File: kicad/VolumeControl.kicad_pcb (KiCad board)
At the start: 2 copper layers, 160 x 59.1 mm, 67 parts, among them IC1 ATMEGA328P-P, P1 PWR_IN, P10 ICSP, P2 SOURCE_1, P3 SOURCE_2, P4 RS232, P5 VOL_KNOB, P6 PI_PWR, P7 PA_EN, P8 FRONT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

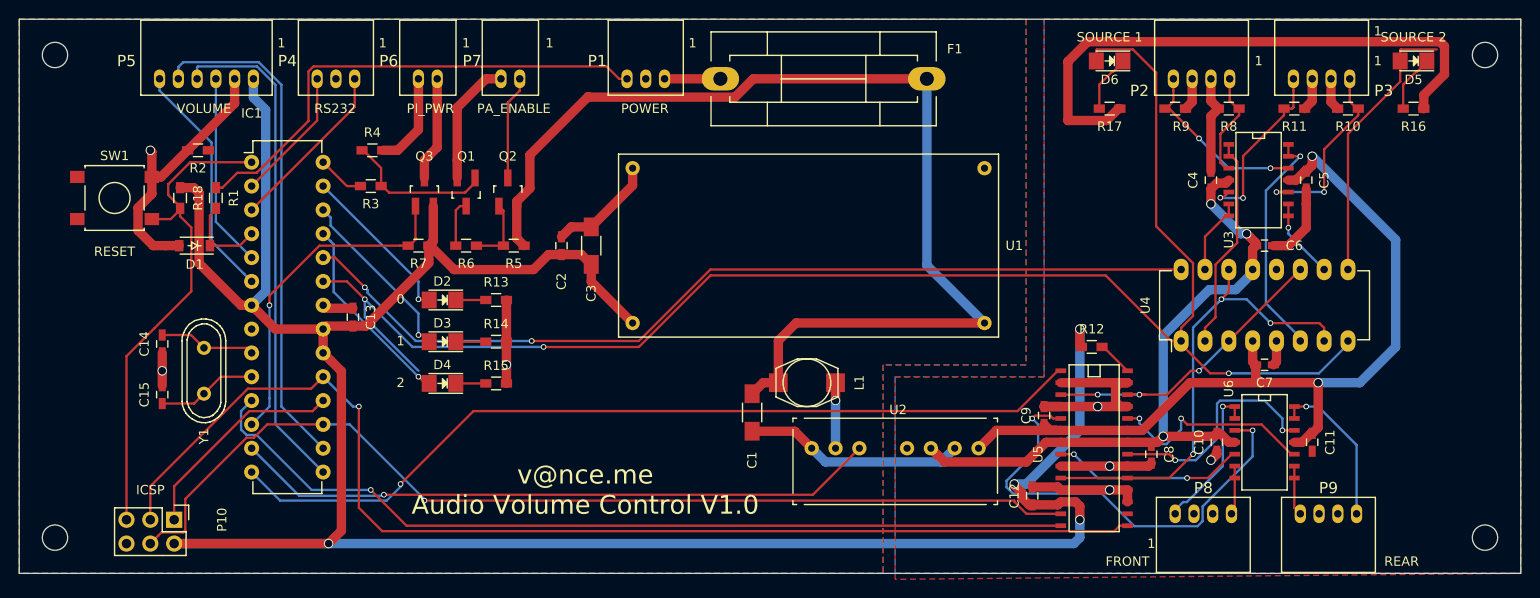
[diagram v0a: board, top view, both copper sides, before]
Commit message: Updated to include extra indicator LEDs controlled by the ATMega.  PCB reworked
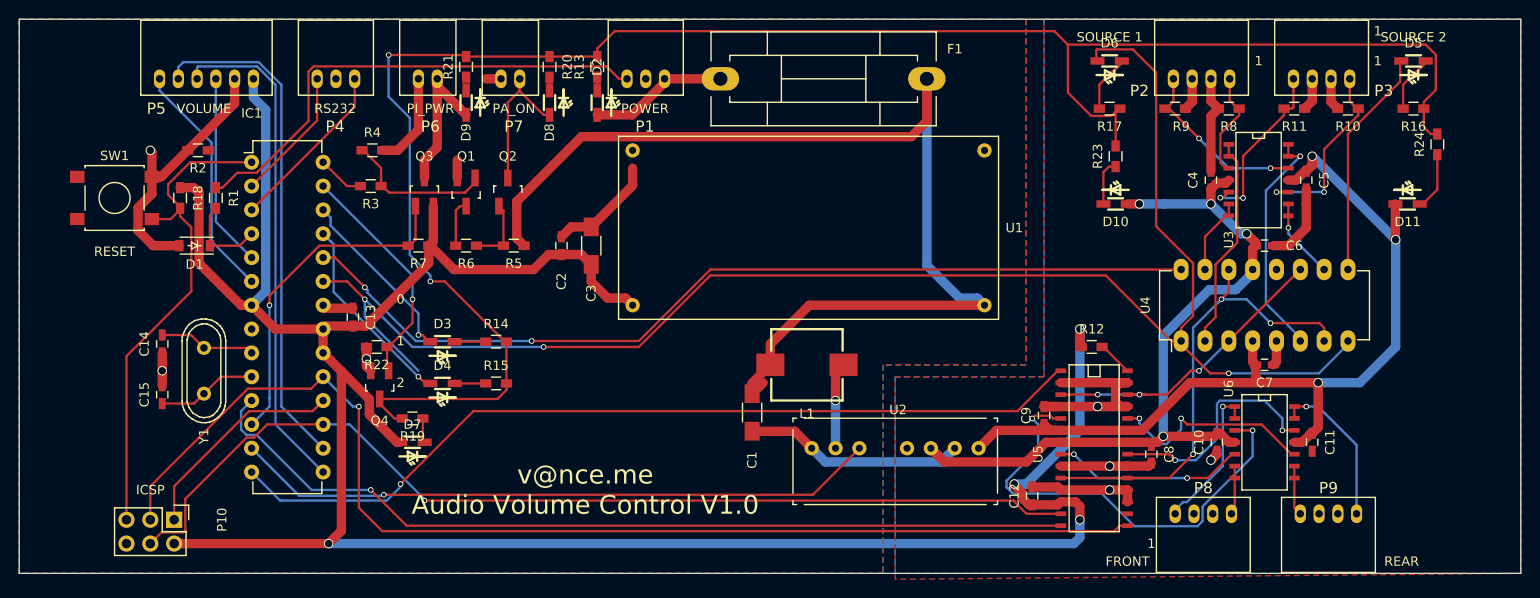
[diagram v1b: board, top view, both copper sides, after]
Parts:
- removed REF** (x4): MountingHole_2.7mm_M2.5_ISO7380, Mounting_Holes:MountingHole_2.7mm_M2.5_ISO7380
- added D10: +5VA, SMD_LED:LED_SMD_1.6x0.8mm, F.Cu at (173.4, 70.5)
- added D11: -5VA, SMD_LED:LED_SMD_1.6x0.8mm, F.Cu at (204.5, 70.5)
- added D7: +5VD, SMD_LED:LED_SMD_1.6x0.8mm, F.Cu at (98.4, 95.9)
- added D8: PA, SMD_LED:LED_SMD_1.6x0.8mm, F.Cu at (113.0, 59.7)
- added D9: PI, SMD_LED:LED_SMD_1.6x0.8mm, F.Cu at (104.1, 59.7)
- added Q4: NXP2301P, TO_SOT_Packages_SMD:SOT-23_Handsoldering, F.Cu at (94.9, 89.8)
- added R19: 220, Resistors_SMD:R_0603_HandSoldering, F.Cu at (98.4, 93.3)
- added R20: 1k, Resistors_SMD:R_0603_HandSoldering, F.Cu at (113.0, 55.9)
- added R21: 220, Resistors_SMD:R_0603_HandSoldering, F.Cu at (104.1, 55.9)
- added R22: 10k, Resistors_SMD:R_0603_HandSoldering, F.Cu at (94.6, 85.7)
- added R23: 220, Resistors_SMD:R_0603_HandSoldering, F.Cu at (173.4, 65.4)
- added R24: 220, Resistors_SMD:R_0603_HandSoldering, F.Cu at (207.6, 64.1)
- D2: value 0 -> +12V; footprint LEDs:LED_1206 -> SMD_LED:LED_SMD_1.6x0.8mm
- D3, D4, D5, D6: footprint LEDs:LED_1206 -> SMD_LED:LED_SMD_1.6x0.8mm
- L1: footprint Inductors:SELF-WE-PD3S -> Inductor_SRR0735A:Inductor_SRR0735A
- Q2, Q3: value Si2301BDS -> NX2301P
- R13: value 220 -> 1k
- moved R13 27.1 mm to (118.1, 55.9), turned to 90 degrees
- moved D2 26.7 mm to (118.1, 59.7), turned to 270 degrees
- moved L1 1.91 mm to (140.5, 87.6)
- moved U1 1.89 mm to (141.4, 81.3)
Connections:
- D2 pad 2: Net-(D2-Pad2) -> /Power/+12V_SUPPLY
- IC1 pad 27: Net-(D2-Pad2) -> Net-(IC1-Pad27)
- R13 pad 2: GND -> LED_GND
- R14 pad 2: GND -> LED_GND
- R15 pad 2: GND -> LED_GND
- R16 pad 2: GND -> LED_GND
- R17 pad 2: GND -> LED_GND
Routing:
- net LED_GND: track 0.00 -> 199.8 mm, vias 0 -> 2
- net GND: track 241.6 -> 164.3 mm
- net Net-(IC1-Pad27): track 0.00 -> 24.9 mm, vias 0 -> 1
- net Net-(D2-Pad2): track 17.4 -> 0.00 mm, vias 1 -> 0
- net /Power/+12V_SUPPLY: track 5.95 -> 15.4 mm
- net +5VA: track 71.4 -> 80.2 mm, vias 3 -> 4
- net Net-(D11-Pad2): track 0.00 -> 6.23 mm
- net +5VD: track 270.7 -> 265.1 mm
- net /Power/+12V_PA_ENABLE: track 11.1 -> 16.6 mm
- net /Power/+5V_PI: track 11.1 -> 16.2 mm
- net /Audio Processing/SOURCE_2_ENABLE: track 128.1 -> 123.0 mm
- net Net-(D10-Pad1): track 0.00 -> 4.93 mm
- net -5VA: track 91.4 -> 95.2 mm, vias 2 -> 3
- net Net-(D7-Pad1): track 0.00 -> 2.62 mm
- net Net-(L1-Pad2): track 6.98 -> 9.24 mm
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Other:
- board text added: "PA_ON"
- board text removed: "PA_ENABLE"

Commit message: Minor updates and board submitted for fabrication
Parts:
- added D12: RX, SMD_LED:LED_SMD_1.6x0.8mm, F.Cu at (67.9, 66.0)
- added D13: TX, SMD_LED:LED_SMD_1.6x0.8mm, F.Cu at (67.9, 69.2)
- added D14: MISO, SMD_LED:LED_SMD_1.6x0.8mm, F.Cu at (67.9, 98.4)
- added D15: MOSI, SMD_LED:LED_SMD_1.6x0.8mm, F.Cu at (67.9, 94.6)
- added R25: 220, Resistors_SMD:R_0603_HandSoldering, F.Cu at (63.5, 66.0)
- added R26: 220, Resistors_SMD:R_0603_HandSoldering, F.Cu at (63.5, 69.2)
- added R27: 220, Resistors_SMD:R_0603_HandSoldering, F.Cu at (63.5, 98.4)
- added R28: 220, Resistors_SMD:R_0603_HandSoldering, F.Cu at (63.5, 94.6)
- added REF**: MountingHole_2.7mm_M2.5_ISO7380_Pad, Mounting_Holes:MountingHole_2.7mm_M2.5_ISO7380_Pad, F.Cu at (60.3, 54.6)
- added REF**: MountingHole_2.7mm_M2.5_ISO7380_Pad, Mounting_Holes:MountingHole_2.7mm_M2.5_ISO7380_Pad, F.Cu at (60.3, 106.0)
- added REF**: MountingHole_2.7mm_M2.5_ISO7380_Pad, Mounting_Holes:MountingHole_2.7mm_M2.5_ISO7380_Pad, F.Cu at (212.7, 106.0)
- added REF**: MountingHole_2.7mm_M2.5_ISO7380_Pad, Mounting_Holes:MountingHole_2.7mm_M2.5_ISO7380_Pad, F.Cu at (212.7, 54.6)
- Q4: value NXP2301P -> TSM2302CX
- moved SW1 5.72 mm to (66.7, 75.6)
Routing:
- net LED_GND: track 199.8 -> 286.0 mm, vias 2 -> 5
- net /DIgital_Control/TX_OUT: track 18.5 -> 57.4 mm, vias 0 -> 1
- net /DIgital_Control/RX_IN: track 14.3 -> 45.5 mm, vias 0 -> 1
- net GND: track 164.3 -> 186.9 mm, vias 7 -> 10
- net /Audio Processing/SOURCE_2_ENABLE: track 123.0 -> 145.5 mm, vias 2 -> 3
- net /DIgital_Control/IGNITION: track 9.21 -> 20.9 mm, vias 0 -> 1
- net /Audio Processing/SOURCE_1_ENABLE: track 170.7 -> 160.8 mm
- net /Audio Processing/SDI: track 108.7 -> 118.3 mm, vias 1 -> 3
- net /DIgital_Control/RESET: track 53.1 -> 62.2 mm
- net /DIgital_Control/MISO: track 23.2 -> 28.4 mm, vias 0 -> 2
- net Net-(D15-Pad1): track 0.00 -> 2.05 mm
- net Net-(D14-Pad1): track 0.00 -> 2.05 mm
- net Net-(D13-Pad1): track 0.00 -> 2.05 mm
- net Net-(D12-Pad1): track 0.00 -> 2.05 mm
- net +5VA: track 80.2 -> 81.9 mm
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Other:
- board text added: "+5VA"
- board text added: "+5VD"
- board text added: "-5VA"
- board text added: "MISO"
- board text added: "MOSI"
- board text added: "RX"
- board text added: "TX"
- board text removed: "0"

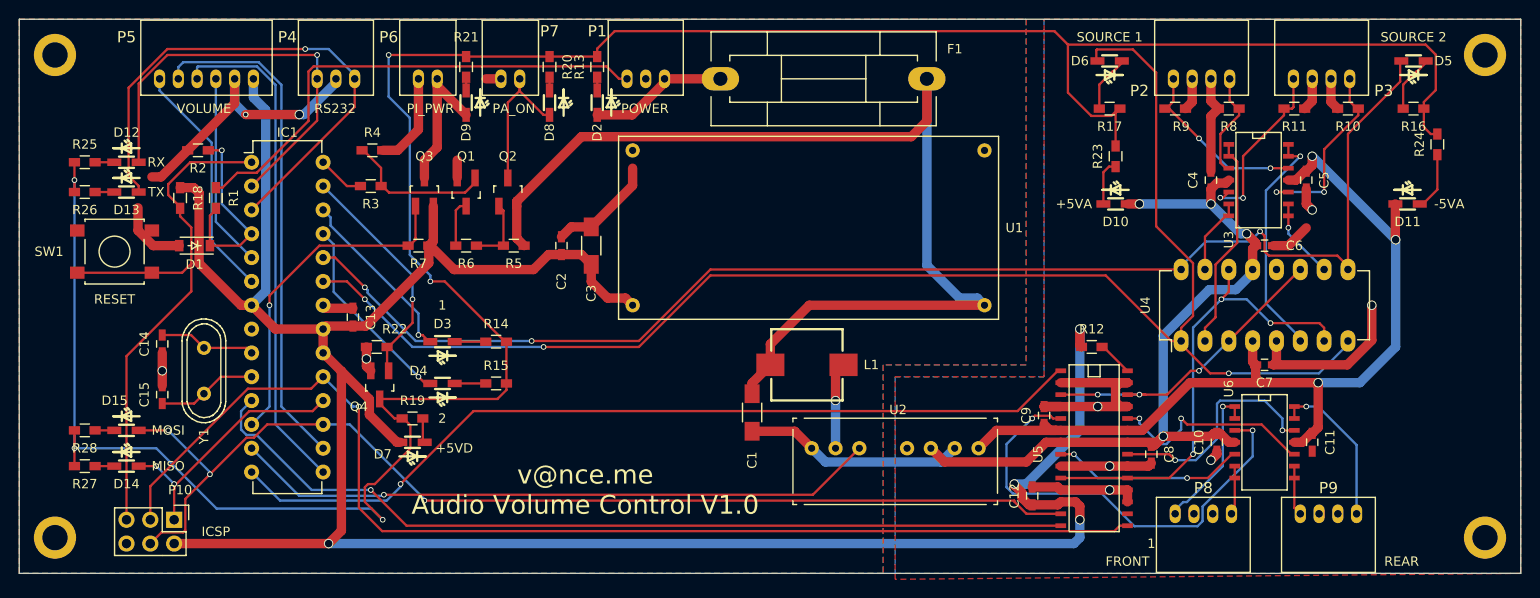
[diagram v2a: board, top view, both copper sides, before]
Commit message: Updated board design with some footprint changes and improved audio layout
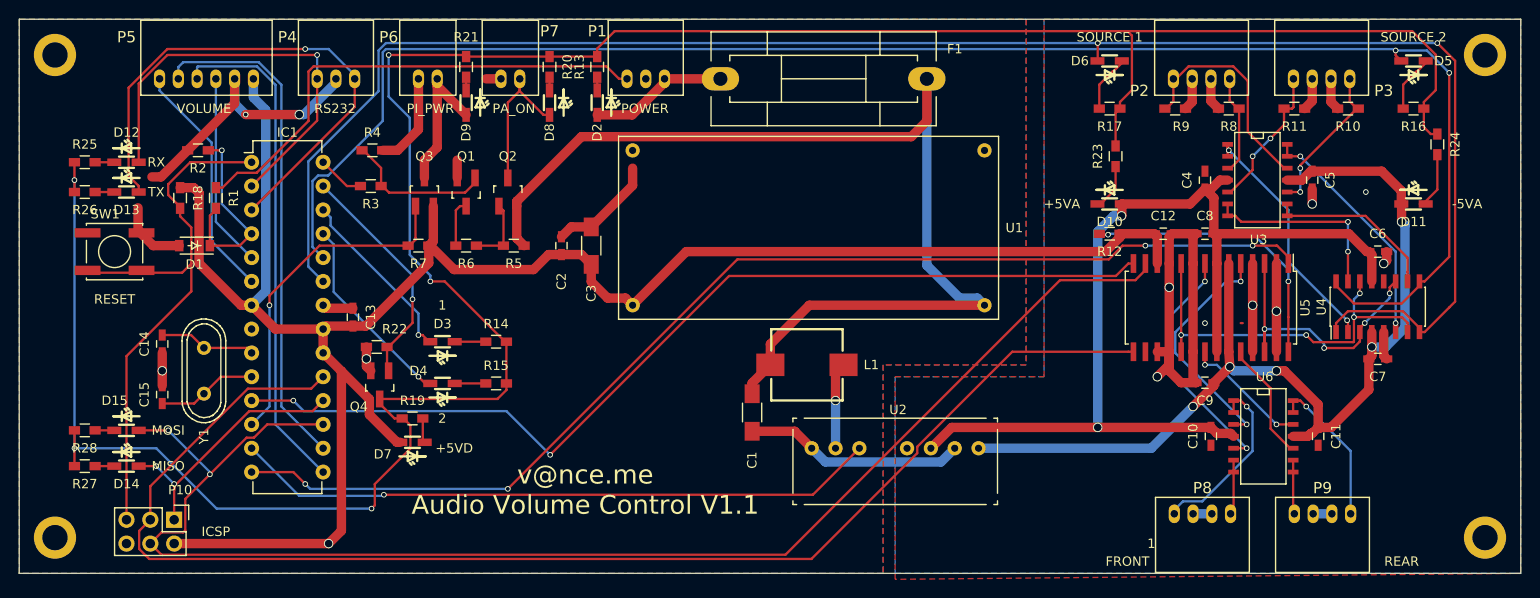
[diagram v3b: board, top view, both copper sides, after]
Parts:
- SW1: footprint Buttons_Switches_SMD:SW_SPST_B3S-1000 -> Buttons_Switches_SMD:SW_SPST_EVPBF
- U4: footprint Housings_DIP:DIP-16_W7.62mm_LongPads -> Housings_SOIC:SOIC-16_3.9x9.9mm_Pitch1.27mm
- U5: footprint SMD_Packages:SOIC-28 -> Housings_SOIC:SOIC-28_7.5x17.9mm_Pitch1.27mm
- moved C12 31.2 mm to (178.4, 73.7), turned to 0 degrees
- moved C8 24.2 mm to (182.9, 73.7), turned to 180 degrees
- moved U4 21.3 mm to (201.3, 81.4)
- moved U5 19.5 mm to (183.5, 81.5)
- moved C9 17.5 mm to (182.9, 89.5), turned to 0 degrees
- moved R12 12.2 mm to (172.7, 73.7), turned to 180 degrees
- moved C6 12.1 mm to (201.3, 75.6)
- moved C7 12.1 mm to (201.3, 87.0)
- moved C10 0.90 mm to (183.5, 95.2)
- moved C11 0.90 mm to (194.9, 95.2)
- moved U6 0.65 mm to (189.2, 95.2)
- moved C4 0.63 mm to (182.9, 67.9)
- moved C5 0.63 mm to (194.3, 67.9)
- moved D10 0.63 mm to (172.7, 70.5)
- moved D11 0.63 mm to (205.1, 70.5)
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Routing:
- net +5VD: track 263.8 -> 211.7 mm, vias 4 -> 1
- net /Audio Processing/SDI: track 118.3 -> 155.1 mm, vias 3 -> 2
- net /Audio Processing/SOURCE_2_ENABLE: track 145.5 -> 177.5 mm, vias 3 -> 2
- net /Audio Processing/MUTE: track 93.4 -> 123.3 mm, vias 1 -> 4
- net +5VA: track 81.9 -> 109.7 mm, vias 4 -> 2
- net /Audio Processing/SOURCE_1_ENABLE: track 160.8 -> 188.5 mm, vias 3 -> 2
- net Net-(R12-Pad2): track 3.76 -> 30.6 mm, vias 0 -> 2
- net Net-(U5-Pad5): track 48.4 -> 25.5 mm
- net /Audio Processing/SCLK: track 125.9 -> 146.4 mm, vias 1 -> 0
- net Net-(U3-Pad6): track 8.22 -> 20.7 mm, vias 0 -> 2
- net Net-(U5-Pad21): track 24.9 -> 13.4 mm
- net Net-(U3-Pad8): track 8.56 -> 18.5 mm, vias 1 -> 0
- net Net-(U5-Pad24): track 22.6 -> 12.8 mm, vias 2 -> 0
- net /Audio Processing/CS: track 95.2 -> 104.8 mm, vias 1 -> 2
- net -5VA: track 95.2 -> 104.0 mm, vias 3 -> 5
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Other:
- board text added: "v@nce.me Audio Volume Control V1.1"
- board text removed: "v@nce.me Audio Volume Control V1.0"
